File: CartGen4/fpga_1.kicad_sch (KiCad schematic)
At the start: 5 parts, among them U9 LFXP2-8E-5MN132C

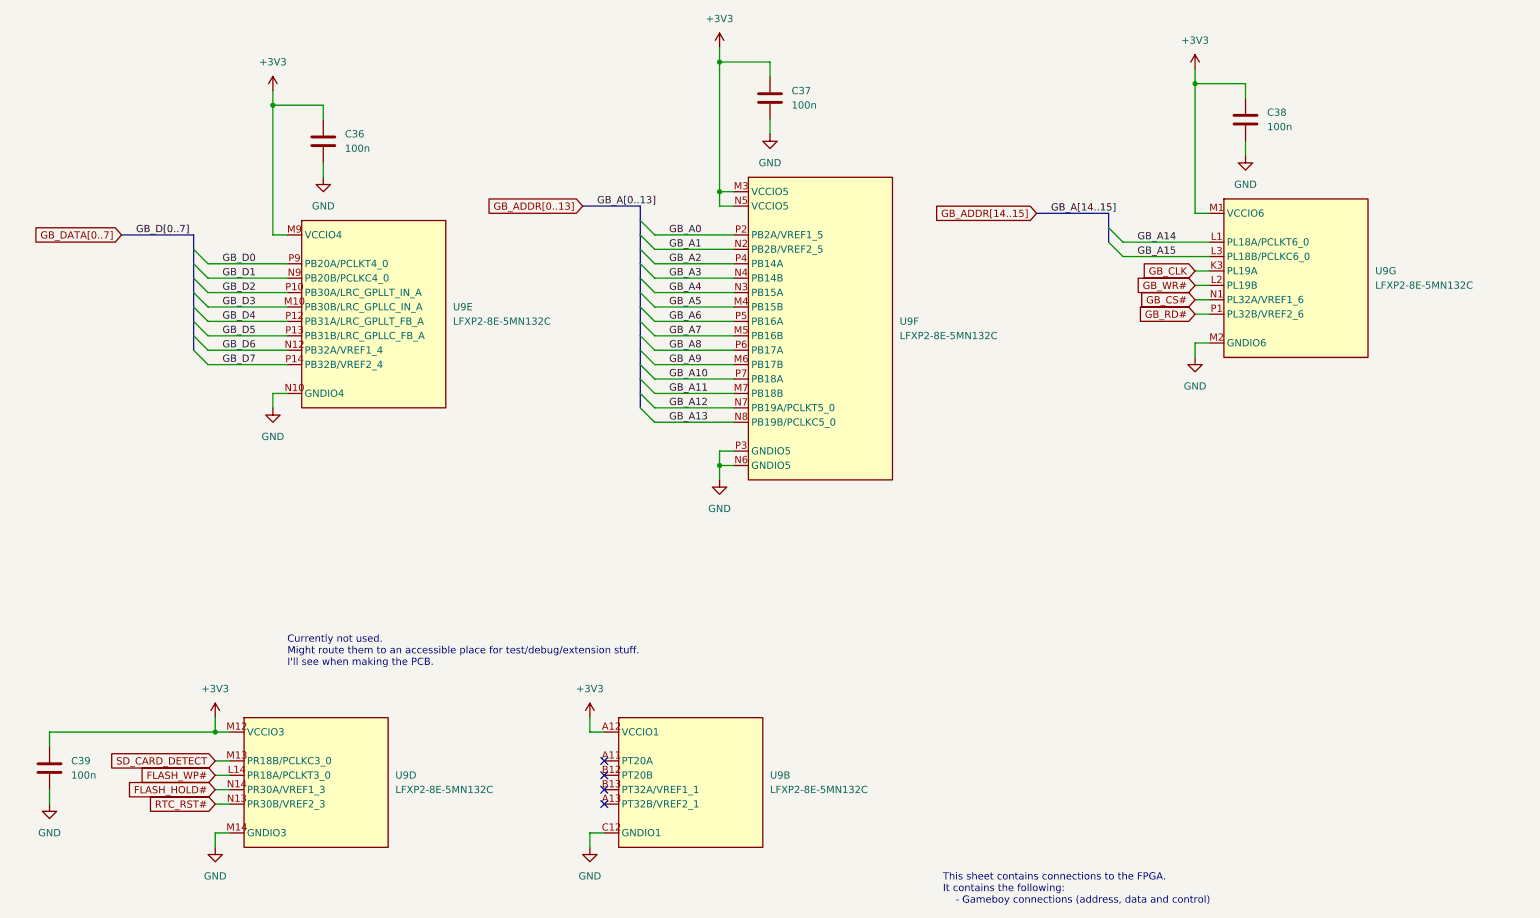
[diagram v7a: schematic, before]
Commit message: Started routing FPGA
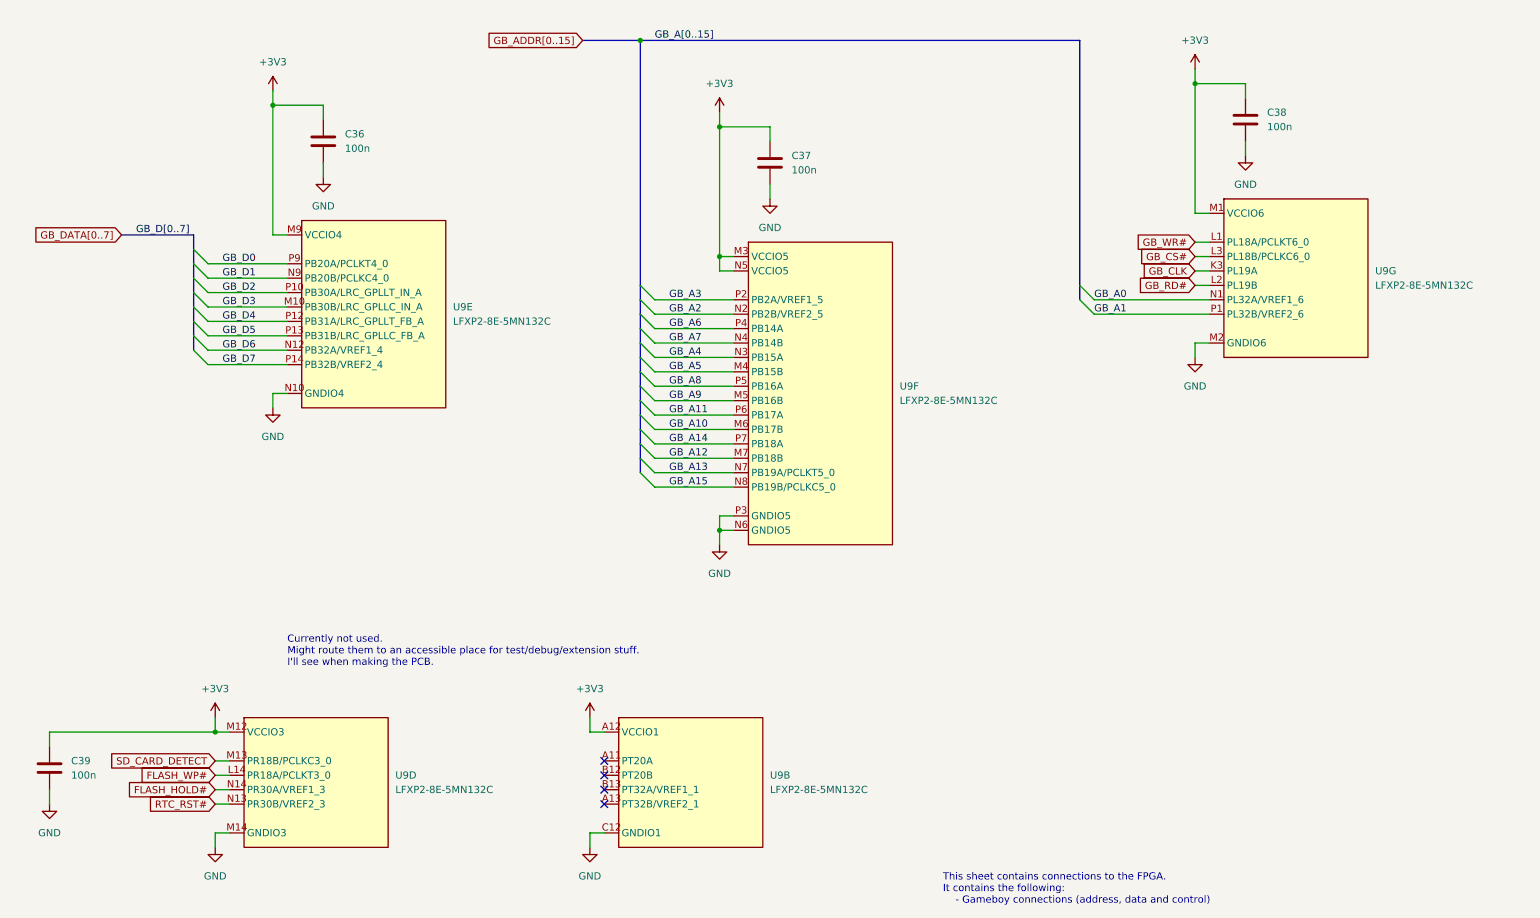
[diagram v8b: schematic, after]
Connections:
- net GB_A0: now also U9.N1 (PL32A/VREF1_6); no longer U9.P2 (PB2A/VREF1_5)
- net GB_A1: now also U9.P1 (PL32B/VREF2_6); no longer U9.N2 (PB2B/VREF2_5)
- net GB_A10: now also U9.M6 (PB17B); no longer U9.P7 (PB18A)
- net GB_A11: now also U9.P6 (PB17A); no longer U9.M7 (PB18B)
- net GB_A12: now also U9.M7 (PB18B); no longer U9.N7 (PB19A/PCLKT5_0)
- net GB_A13: now also U9.N7 (PB19A/PCLKT5_0); no longer U9.N8 (PB19B/PCLKC5_0)
- net GB_A14: now also U9.P7 (PB18A); no longer U9.L1 (PL18A/PCLKT6_0)
- net GB_A15: now also U9.N8 (PB19B/PCLKC5_0); no longer U9.L3 (PL18B/PCLKC6_0)
- net GB_A2: now also U9.N2 (PB2B/VREF2_5); no longer U9.P4 (PB14A)
- net GB_A3: now also U9.P2 (PB2A/VREF1_5); no longer U9.N4 (PB14B)
- net GB_A6: now also U9.P4 (PB14A); no longer U9.P5 (PB16A)
- net GB_A7: now also U9.N4 (PB14B); no longer U9.M5 (PB16B)
- net GB_A8: now also U9.P5 (PB16A); no longer U9.P6 (PB17A)
- net GB_A9: now also U9.M5 (PB16B); no longer U9.M6 (PB17B)
- net GB_CS#: now also U9.L3 (PL18B/PCLKC6_0); no longer U9.N1 (PL32A/VREF1_6)
- net GB_RD#: now also U9.L2 (PL19B); no longer U9.P1 (PL32B/VREF2_6)
- net GB_WR#: now also U9.L1 (PL18A/PCLKT6_0); no longer U9.L2 (PL19B)
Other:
- moved on the sheet: C37, U9F
